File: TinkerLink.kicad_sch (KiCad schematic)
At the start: 28 parts, among them J1 Conn_01x06_Pin, Q2 MMBT2222A, Q3 SQS411ENW-T1_GE3, Q4 SQS411ENW-T1_GE3, SW1 TS-061D-250D4-P, U1 ESP-01F-2M, U2 ME6211C33M5, U3 AP63203WU

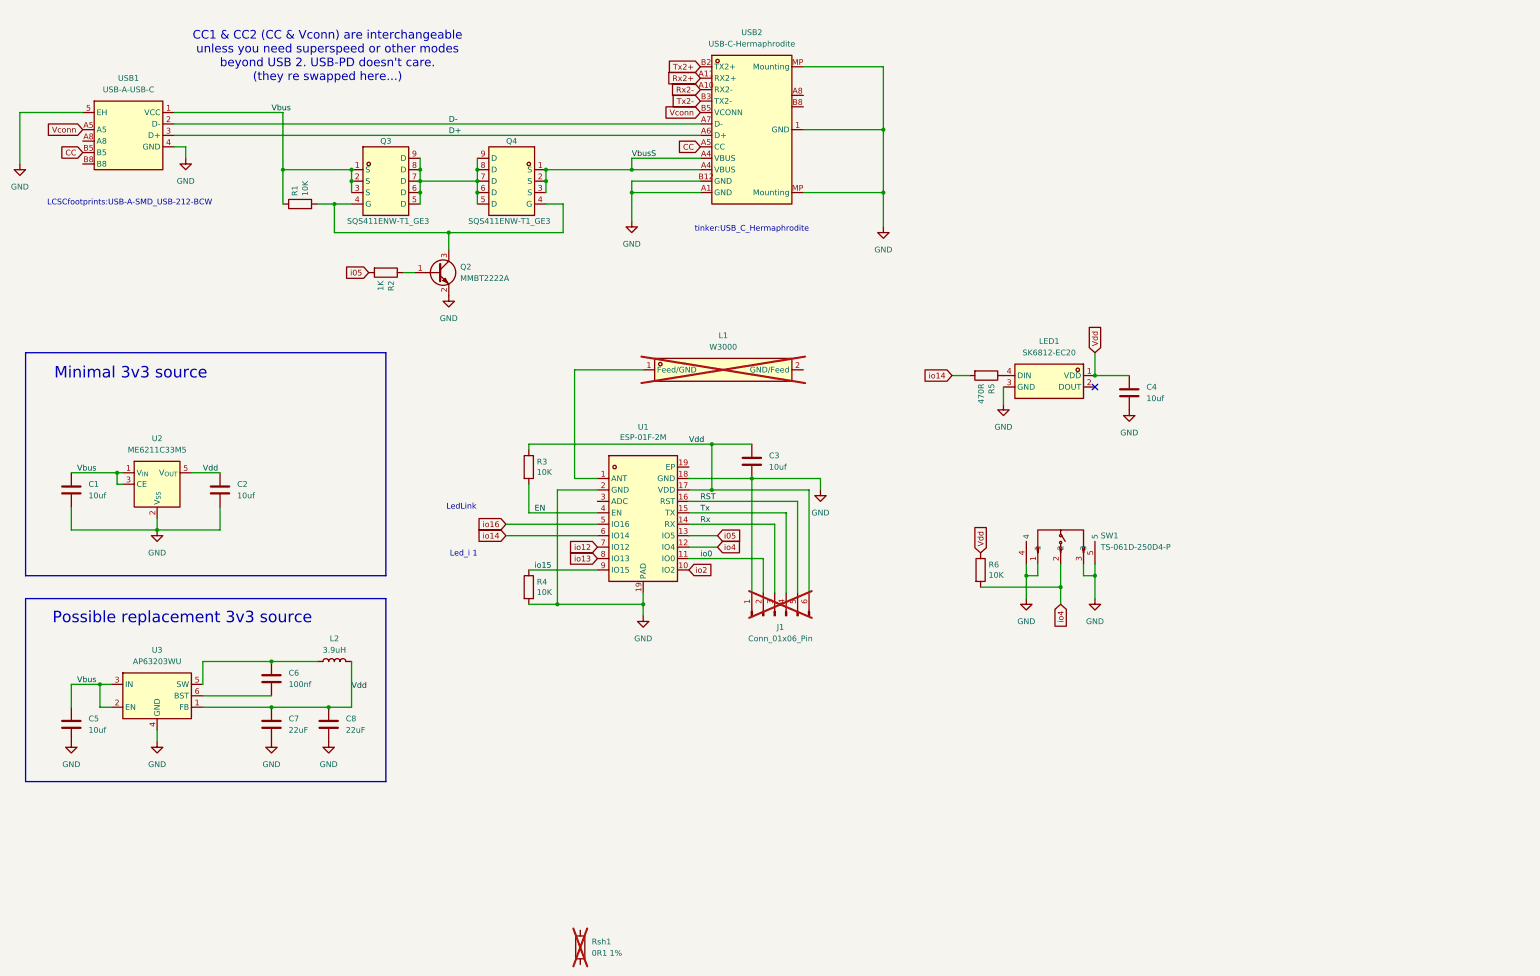
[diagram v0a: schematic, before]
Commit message: upgrades
adds ina228 and 3535 rgbw sk6812 LED
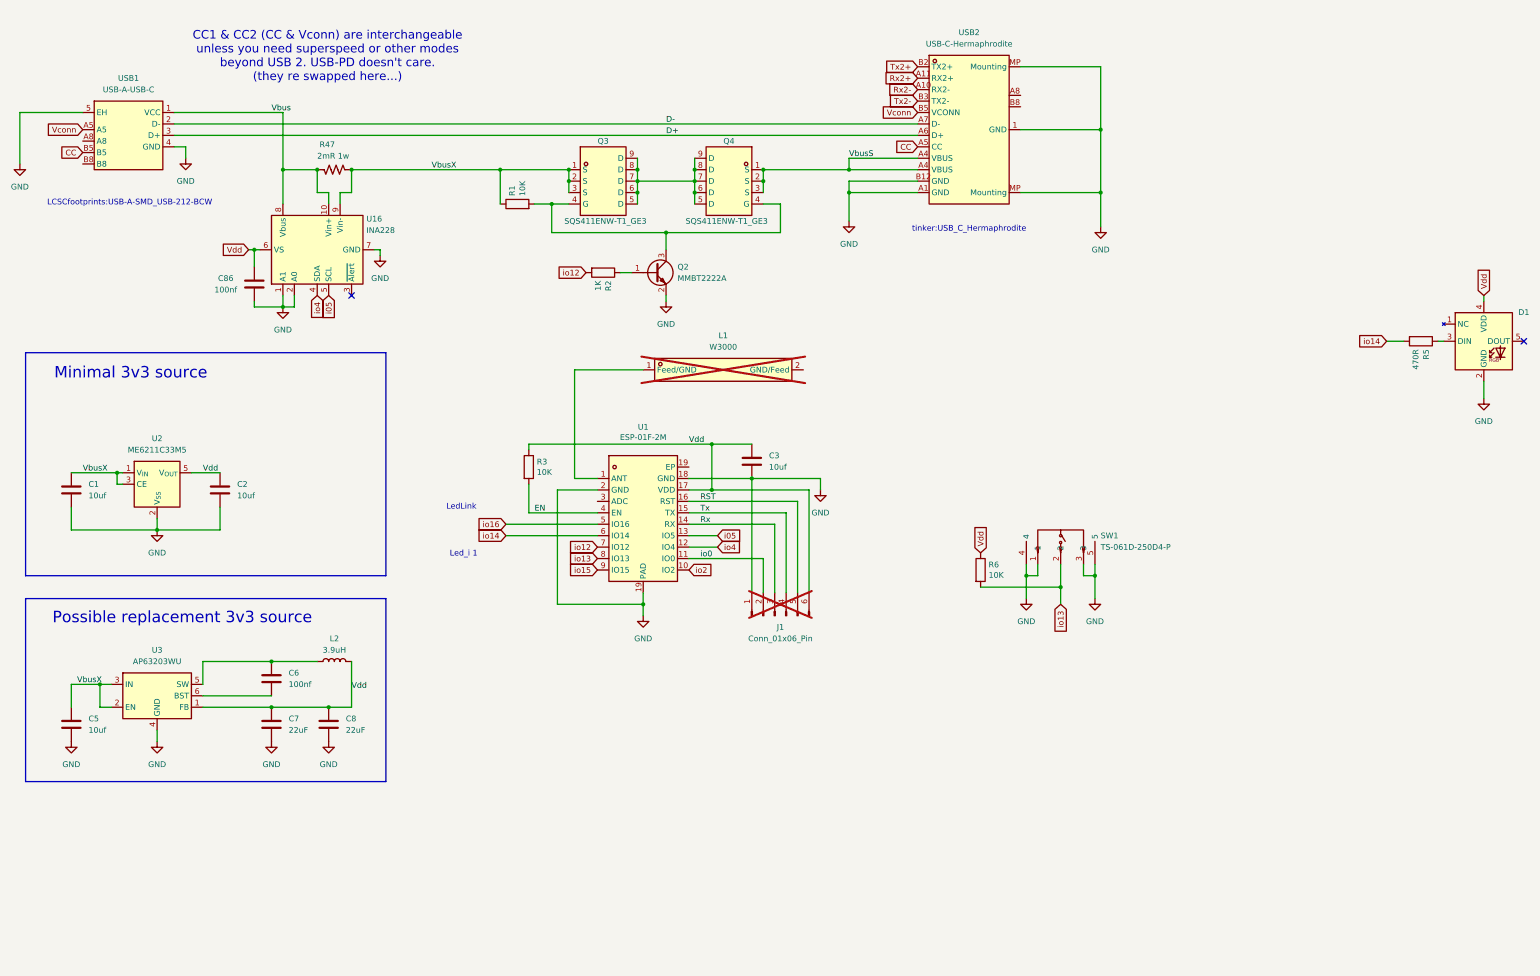
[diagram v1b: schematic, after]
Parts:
- removed C4: 10uf, Capacitor_SMD:C_0603_1608Metric, symbol Device:C
- removed LED1: SK6812-EC20, LCSCfootprints:LED-SMD_4P-L2.0-W2.0-BR, symbol LED-SMD_4P-L2.0-W2.0-BR:SK6812-EC20
- removed R4: 10K, Resistor_SMD:R_0603_1608Metric, symbol Device:R
- removed Rsh1: 0R1 1%, Resistor_SMD:R_2512_6332Metric, symbol Device:R
- added C86: 100nf, Capacitor_SMD:C_0603_1608Metric, symbol Device:C
- added D1: ~, AC_LED:SK6812MINIRGBWNWP6, symbol AC_LED:SK6812_mini_RGBW
- added R47: 2mR 1w, Resistor_SMD:R_1206_3216Metric, symbol Device:R_US
- added U16: INA228, Package_SO:VSSOP-10_3x3mm_P0.5mm, symbol Sensor_Energy:INA228
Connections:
- net GND: now also C86.2, D1.2 (GND), U16.1 (A1), U16.2 (A0), U16.7 (GND)
- net Vbus: now also R47.2, U16.10 (Vin+), U16.8 (Vbus); no longer C1.1, C5.1, Q3.1 (S), Q3.2 (S), Q3.3 (S), R1.1, U2.1 (V_{IN}), U2.3 (CE), U3.2 (EN), U3.3 (IN)
- net Vdd: now also C86.1, D1.4 (VDD), U16.6 (VS)
- net i05: now also U16.5 (SCL); no longer R2.2
- net io12: now also R2.2
- net io13: now also R6.2, SW1.2
- net io4: now also U16.4 (SDA); no longer R6.2, SW1.2
- net at R5.1: now also D1.3 (DIN)
- new net VbusX: C1.1, C5.1, Q3.1 (S), Q3.2 (S), Q3.3 (S), R1.1, R47.1, U16.9 (Vin-), U2.1 (V_{IN}), U2.3 (CE), U3.2 (EN), U3.3 (IN)
- no-connect marks 1 -> 2
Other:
- moved on the sheet: Q2, Q3, Q4, R1, R2, R5, USB2

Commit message: add AC logo
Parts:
- added LOGO1: Creations_logo_med, AC_logos:Creations logo med, symbol AC_logos:Creations_logo_med
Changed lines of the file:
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@@
+	)
+	(symbol
+		(lib_id "AC_logos:Creations_logo_med")
+		(at 19.05 20.32 0)
+		(unit 1)
+		(exclude_from_sim no)
+		(in_bom yes)
+		(on_board yes)
+		(dnp no)
+		(fields_autoplaced yes)
+		(property "Reference" "LOGO1"
+			(at 21.59 19.3039 0)
+			(effects
+				(font
+					(size 1.27 1.27)
+				)
+				(justify left)
+			)
+		)
+		(property "Value" "Creations_logo_med"
+			(at 21.59 21.8439 0)
+			(effects
+				(font
+					(size 1.27 1.27)
+				)
+				(justify left)
+			)
+		)
+		(property "Footprint" "AC_logos:Creations logo med"
+			(at 35.814 23.876 0)
+			(effects
+				(font
+					(size 1.27 1.27)
+				)
+				(hide yes)
+			)
+		)
+		(property "Datasheet" ""
+			(at 19.05 20.32 0)
+			(effects
+				(font
+					(size 1.27 1.27)
+				)
+				(hide yes)
+			)
+		)
+		(property "Description" ""
+			(at 19.05 20.32 0)
+			(effects
+				(font
+					(size 1.27 1.27)
+				)
+				(hide yes)
+			)
+		)
+		(instances
+			(project ""
+				(path "/d9db63b9-0e33-4ffc-b3bb-ae5011fef151"
+					(reference "LOGO1")
+					(unit 1)
+				)
+			)
+		)
 	)
 	(symbol

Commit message: first tweaks post Austin...
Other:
- company: (none) -> S. A. Miller
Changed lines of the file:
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@@
 	(title_block
 		(title "TinkerLink")
-		(rev "0.0.5")
+		(rev "0.0.6")
+		(company "S. A. Miller")
+		(comment 1 "With much input by Austin McNeal")
 	)
 	(rectangle

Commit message: ...
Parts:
- added LED1: SK6812MINIRGBW-WS-P6-A, LCSCfootprints:LED-SMD_6P-L3.5-W3.5_SK6812MINIRGBW-WS-P6-A, symbol C7423106:SK6812MINIRGBW-WS-P6-A
- D1: footprint AC_LED:SK6812MINIRGBWNWP6 -> LCSCfootprints:LED-SMD_6P-L3.5-W3.5_SK6812MINIRGBW-WS-P6-A; now not fitted
- LOGO1: footprint AC_logos:Creations logo med -> LCSCfootprints:Creations logo med
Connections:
- net GND: now also LED1.2 (GND); no longer D1.2 (GND)
- net Vdd: now also LED1.4 (VDD), LED1.6 (VDD); no longer D1.4 (VDD)
- net at R5.1: now also LED1.3 (DIN); no longer D1.3 (DIN)
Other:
- moved on the sheet: R5
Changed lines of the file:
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@@
 	)
 	(junction
+		(at 261.62 93.98)
+		(diameter 0)
+		(color 0 0 0 0)
+	)
+	(junction
 		(at 40.64 115.57)
 		(diameter 0)
@@
 	)
 	(no_connect
-		(at 353.06 86.36)
+		(at 237.49 93.98)
 	)
 	(no_connect
@@
 	(wire
 		(pts
-			(xy 322.58 86.36) (xy 326.39 86.36)
+			(xy 220.98 99.06) (xy 224.79 99.06)
 		)
 		(stroke
@@
 	(wire
 		(pts
+			(xy 236.22 96.52) (xy 236.22 106.68)
+		)
+		(stroke
+			(width 0)
+			(type default)
+		)
+	)
+	(wire
+		(pts
 			(xy 77.47 78.74) (xy 80.01 78.74)
 		)
@@
 	(wire
 		(pts
+			(xy 261.62 99.06) (xy 261.62 93.98)
+		)
+		(stroke
+			(width 0)
+			(type default)
+		)
+	)
+	(wire
+		(pts
 			(xy 77.47 76.2) (xy 77.47 78.74)
 		)
@@
 	(wire
 		(pts
-			(xy 334.01 86.36) (xy 335.28 86.36)
+			(xy 232.41 99.06) (xy 237.49 99.06)
 		)
 		(stroke
@@
 	(wire
 		(pts
+			(xy 257.81 99.06) (xy 261.62 99.06)
+		)
+		(stroke
+			(width 0)
+			(type default)
+		)
+	)
+	(wire
+		(pts
 			(xy 184.15 142.24) (xy 184.15 134.62)
 		)
@@
 	(wire
 		(pts
-			(xy 344.17 76.2) (xy 344.17 77.47)
+			(xy 265.43 93.98) (xy 261.62 93.98)
 		)
 		(stroke
@@
 	(wire
 		(pts
+			(xy 261.62 93.98) (xy 257.81 93.98)
+		)
+		(stroke
+			(width 0)
+			(type default)
+		)
+	)
+	(wire
+		(pts
 			(xy 125.73 48.26) (xy 125.73 55.88)
 		)
@@
 	(wire
 		(pts
+			(xy 237.49 96.52) (xy 236.22 96.52)
+		)
+		(stroke
+			(width 0)
+			(type default)
+		)
+	)
+	(wire
+		(pts
 			(xy 30.48 128.27) (xy 30.48 123.19)
 		)
@@
 	(wire
 		(pts
-			(xy 344.17 95.25) (xy 344.17 99.06)
-		)
-		(stroke
-			(width 0)
-			(type default)
-		)
-	)
-	(wire
-		(pts
 			(xy 71.12 77.47) (xy 71.12 78.74)
 		)
@@
 	(global_label "io14"
 		(shape input)
-		(at 322.58 86.36 180)
+		(at 220.98 99.06 180)
 		(fields_autoplaced yes)
 		(effects
@@
 		)
 		(property "Intersheetrefs" "${INTERSHEET_REFS}"
-			(at 315.422 86.36 0)
+			(at 213.822 99.06 0)
 			(effects
 				(font
@@
 	(global_label "Vdd"
 		(shape input)
-		(at 344.17 76.2 90)
+		(at 265.43 93.98 0)
 		(fields_autoplaced yes)
 		(effects
@@
 		)
 		(property "Intersheetrefs" "${INTERSHEET_REFS}"
-			(at 344.17 69.8282 90)
+			(at 271.8018 93.98 0)
 			(effects
 				(font
@@
 	)
 	(symbol
+		(lib_id "C7423106:SK6812MINIRGBW-WS-P6-A")
+		(at 247.65 96.52 0)
+		(unit 1)
+		(exclude_from_sim no)
+		(in_bom yes)
+		(on_board yes)
+		(dnp no)
+		(fields_autoplaced yes)
+		(property "Reference" "LED1"
+			(at 247.65 86.36 0)
+			(effects
+				(font
+					(size 1.27 1.27)
+				)
+			)
+		)
+		(property "Value" "SK6812MINIRGBW-WS-P6-A"
+			(at 247.65 88.9 0)
+			(effects
+				(font
+					(size 1.27 1.27)
+				)
+			)
+		)
+		(property "Footprint" "LCSCfootprints:LED-SMD_6P-L3.5-W3.5_SK6812MINIRGBW-WS-P6-A"
+			(at 247.65 106.68 0)
+			(effects
+				(font
+					(size 1.27 1.27)
+				)
+				(hide yes)
+			)
+		)
+		(property "Datasheet" "https://www.lcsc.com/datasheet/C7423106.pdf"
+			(at 247.65 109.22 0)
+			(effects
+				(font
+					(size 1.27 1.27)
+				)
+				(hide yes)
+			)
+		)
+		(property "Description" ""
+			(at 247.65 96.52 0)
+			(effects
+				(font
+					(size 1.27 1.27)
+				)
+				(hide yes)
+			)
+		)
+		(property "Manufacturer" "OPSCO(欧思科)"
+			(at 247.65 111.76 0)
+			(effects
+				(font
+					(size 1.27 1.27)
+				)
+				(hide yes)
+			)
+		)
+		(property "MPN" "SK6812MINIRGBW-WS-P6-A"
+			(at 247.65 114.3 0)
+			(effects
+				(font
+					(size 1.27 1.27)
+				)
+				(hide yes)
+			)
+		)
+		(property "LCSC Part" "C7423106"
+			(at 247.65 116.84 0)
+			(effects
+				(font
+					(size 1.27 1.27)
+				)
+				(hide yes)
+			)
+		)
+		(pin "2"
+		)
+		(pin "4"
+		)
+		(pin "3"
+		)
+		(pin "1"
+		)
+		(pin "6"
+		)
+		(pin "5"
+		)
+		(instances
+			(project ""
+				(path "/d9db63b9-0e33-4ffc-b3bb-ae5011fef151"
+					(reference "LED1")
+					(unit 1)
+				)
+			)
+		)
+	)
+	(symbol
 		(lib_id "power:GND")
 		(at 30.48 175.26 0)
@@
 			)
 		)
-		(property "Footprint" "AC_logos:Creations logo med"
+		(property "Footprint" "LCSCfootprints:Creations logo med"
 			(at 35.814 23.876 0)
 			(effects
@@
 	(symbol
 		(lib_id "AC_LED:SK6812_mini_RGBW")
-		(at 344.17 86.36 0)
+		(at 298.45 95.25 0)
 		(unit 1)
 		(exclude_from_sim no)
 		(in_bom yes)
-		(on_board yes)
-		(dnp no)
+		(on_board no)
+		(dnp yes)
 		(fields_autoplaced yes)
 		(property "Reference" "D1"
-			(at 353.06 79.9398 0)
+			(at 307.34 88.8298 0)
 			(effects
 				(font
@@
 		)
 		(property "Value" "~"
-			(at 353.06 82.4798 0)
+			(at 307.34 91.3698 0)
 			(effects
 				(font
@@
 			)
 		)
-		(property "Footprint" "AC_LED:SK6812MINIRGBWNWP6"
-			(at 343.916 108.966 0)
+		(property "Footprint" "LCSCfootprints:LED-SMD_6P-L3.5-W3.5_SK6812MINIRGBW-WS-P6-A"
+			(at 298.196 117.856 0)
 			(effects
 				(font
@@
 		)
 		(property "Datasheet" ""
-			(at 344.17 86.36 0)
+			(at 298.45 95.25 0)
 			(effects
 				(font
@@
 		)
 		(property "Description" "3535 rgbw sk6812 led"
-			(at 344.424 106.68 0)
+			(at 298.704 115.57 0)
 			(effects
 				(font
@@
 		)
 		(property "LCSC" "C7423106"
-			(at 344.17 86.36 0)
+			(at 298.45 95.25 0)
 			(effects
 				(font
@@
 		)
 		(property "warm white" "C7423106"
-			(at 344.17 86.36 0)
+			(at 298.45 95.25 0)
 			(effects
 				(font
@@
 		)
 		(property "cold white" "C7423105"
-			(at 344.17 86.36 0)
+			(at 298.45 95.25 0)
 			(effects
 				(font
@@
 		)
 		(property "neutral white" "C7423107"
-			(at 344.17 86.36 0)
+			(at 298.45 95.25 0)
 			(effects
 				(font
@@
 	(symbol
 		(lib_id "Device:R")
-		(at 330.2 86.36 270)
+		(at 228.6 99.06 270)
 		(unit 1)
 		(exclude_from_sim no)
@@
 		(dnp no)
 		(property "Reference" "R5"
-			(at 331.3684 88.138 0)
+			(at 229.7684 100.838 0)
 			(effects
 				(font
@@
 		)
 		(property "Value" "470R"
-			(at 329.057 88.138 0)
+			(at 227.457 100.838 0)
 			(effects
 				(font
@@
 		)
 		(property "Footprint" "Resistor_SMD:R_0603_1608Metric"
-			(at 330.2 84.582 90)
+			(at 228.6 97.282 90)
 			(effects
 				(font
@@
 		)
 		(property "Datasheet" "~"
-			(at 330.2 86.36 0)
+			(at 228.6 99.06 0)
 			(effects
 				(font
@@
 		)
 		(property "Description" ""
-			(at 330.2 86.36 0)
+			(at 228.6 99.06 0)
 			(effects
 				(font
@@
 		)
 		(property "LCSC Part" "C114433"
-			(at 330.2 86.36 0)
+			(at 228.6 99.06 0)
 			(effects
 				(font
@@
 	(symbol
 		(lib_id "power:GND")
-		(at 344.17 99.06 0)
+		(at 236.22 106.68 0)
 		(unit 1)
 		(exclude_from_sim no)
@@
 		(fields_autoplaced yes)
 		(property "Reference" "#PWR017"
-			(at 344.17 105.41 0)
+			(at 236.22 113.03 0)
 			(effects
 				(font
@@
 		)
 		(property "Value" "GND"
-			(at 344.17 104.14 0)
+			(at 236.22 111.76 0)
 			(effects
 				(font
@@
 		)
 		(property "Footprint" ""
-			(at 344.17 99.06 0)
+			(at 236.22 106.68 0)
 			(effects
 				(font
@@
 		)
 		(property "Datasheet" ""
-			(at 344.17 99.06 0)
+			(at 236.22 106.68 0)
 			(effects
 				(font
@@
 		)
 		(property "Description" "Power symbol creates a global label with name \"GND\" , ground"
-			(at 344.17 99.06 0)
+			(at 236.22 106.68 0)
 			(effects
 				(font

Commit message: ...
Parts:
- LOGO1: footprint LCSCfootprints:Creations logo med -> AUSTINfootprints:Creations logo med
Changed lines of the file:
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@@
 			)
 		)
-		(property "Footprint" "LCSCfootprints:Creations logo med"
+		(property "Footprint" "AUSTINfootprints:Creations logo med"
 			(at 35.814 23.876 0)
 			(effects

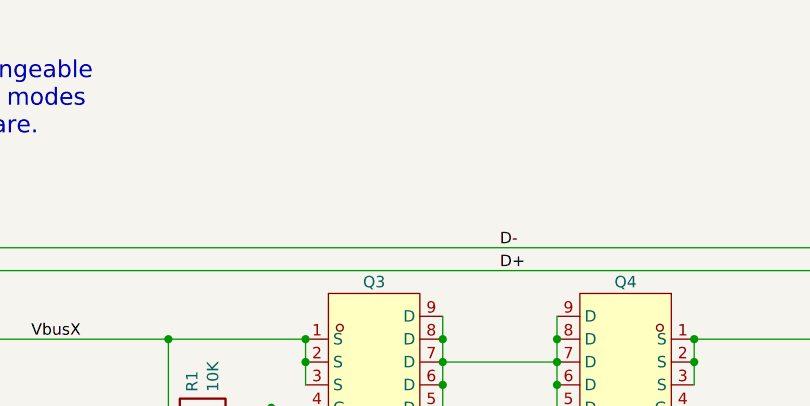
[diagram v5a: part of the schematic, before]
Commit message: Added TPD2EUSB30A to D+/D- for ESD protection
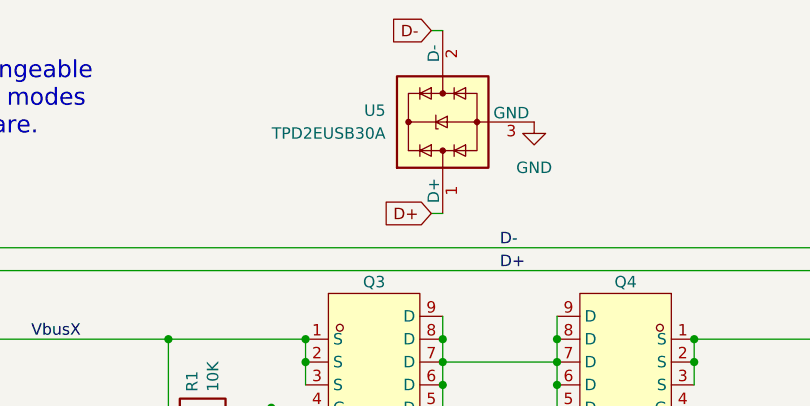
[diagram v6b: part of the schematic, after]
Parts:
- added U5: TPD2EUSB30A, Package_TO_SOT_SMD:Texas_DRT-3, symbol Power_Protection:TPD2EUSB30A
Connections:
- net D+: now also U5.1 (D+)
- net D-: now also U5.2 (D-)
- net GND: now also U5.3 (GND)
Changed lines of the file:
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@@
 	(wire
 		(pts
+			(xy 154.94 34.29) (xy 156.21 34.29)
+		)
+		(stroke
+			(width 0)
+			(type default)
+		)
+	)
+	(wire
+		(pts
 			(xy 156.21 53.34) (xy 156.21 55.88)
 		)
@@
 	(wire
 		(pts
+			(xy 154.94 13.97) (xy 156.21 13.97)
+		)
+		(stroke
+			(width 0)
+			(type default)
+		)
+	)
+	(wire
+		(pts
 			(xy 87.63 167.64) (xy 92.71 167.64)
 		)
@@
 		)
 	)
+	(global_label "D-"
+		(shape input)
+		(at 154.94 13.97 180)
+		(fields_autoplaced yes)
+		(effects
+			(font
+				(size 1.27 1.27)
+			)
+			(justify right)
+		)
+		(property "Intersheetrefs" "${INTERSHEET_REFS}"
+			(at 149.1124 13.97 0)
+			(effects
+				(font
+					(size 1.27 1.27)
+				)
+				(justify right)
+				(hide yes)
+			)
+		)
+	)
 	(global_label "CC"
 		(shape input)
@@
 		)
 	)
+	(global_label "D+"
+		(shape input)
+		(at 154.94 34.29 180)
+		(fields_autoplaced yes)
+		(effects
+			(font
+				(size 1.27 1.27)
+			)
+			(justify right)
+		)
+		(property "Intersheetrefs" "${INTERSHEET_REFS}"
+			(at 149.1124 34.29 0)
+			(effects
+				(font
+					(size 1.27 1.27)
+				)
+				(justify right)
+				(hide yes)
+			)
+		)
+	)
 	(global_label "io16"
 		(shape input)
@@
 	(symbol
 		(lib_id "power:GND")
+		(at 166.37 24.13 0)
+		(unit 1)
+		(exclude_from_sim no)
+		(in_bom yes)
+		(on_board yes)
+		(dnp no)
+		(fields_autoplaced yes)
+		(property "Reference" "#PWR022"
+			(at 166.37 30.48 0)
+			(effects
+				(font
+					(size 1.27 1.27)
+				)
+				(hide yes)
+			)
+		)
+		(property "Value" "GND"
+			(at 166.37 29.21 0)
+			(effects
+				(font
+					(size 1.27 1.27)
+				)
+			)
+		)
+		(property "Footprint" ""
+			(at 166.37 24.13 0)
+			(effects
+				(font
+					(size 1.27 1.27)
+				)
+				(hide yes)
+			)
+		)
+		(property "Datasheet" ""
+			(at 166.37 24.13 0)
+			(effects
+				(font
+					(size 1.27 1.27)
+				)
+				(hide yes)
+			)
+		)
+		(property "Description" "Power symbol creates a global label with name \"GND\" , ground"
+			(at 166.37 24.13 0)
+			(effects
+				(font
+					(size 1.27 1.27)
+				)
+				(hide yes)
+			)
+		)
+		(pin "1"
+		)
+		(instances
+			(project "TinkerLink"
+				(path "/d9db63b9-0e33-4ffc-b3bb-ae5011fef151"
+					(reference "#PWR022")
+					(unit 1)
+				)
+			)
+		)
+	)
+	(symbol
+		(lib_id "power:GND")
 		(at 162.56 77.47 0)
 		(unit 1)
@@
 					(unit 1)
 				)
+			)
+		)
+	)
+	(symbol
+		(lib_id "Power_Protection:TPD2EUSB30A")
+		(at 156.21 24.13 90)
+		(unit 1)
+		(exclude_from_sim no)
+		(in_bom yes)
+		(on_board yes)
+		(dnp no)
+		(property "Reference" "U5"
+			(at 149.86 22.8599 90)
+			(effects
+				(font
+					(size 1.27 1.27)
+				)
+				(justify left)
+			)
+		)
+		(property "Value" "TPD2EUSB30A"
+			(at 149.86 25.3999 90)
+			(effects
+				(font
+					(size 1.27 1.27)
+				)
+				(justify left)
+			)
+		)
+		(property "Footprint" "Package_TO_SOT_SMD:Texas_DRT-3"
+			(at 163.83 43.18 0)
+			(effects
+				(font
+					(size 1.27 1.27)
+				)
+				(hide yes)
+			)
+		)
+		(property "Datasheet" "http://www.ti.com/lit/ds/symlink/tpd2eusb30a.pdf"
+			(at 156.21 24.13 0)
+			(effects
+				(font
+					(size 1.27 1.27)
+				)
+				(hide yes)
+			)
+		)
+		(property "Description" "2-Channel ESD Protection for Super-Speed USB 3.0 Interface, DRT-3"
+			(at 156.21 24.13 0)
+			(effects
+				(font
+					(size 1.27 1.27)
+				)
+				(hide yes)
+			)
+		)
+		(property "LCSC Part" "C3011197"
+			(at 156.21 24.13 90)
+			(effects
+				(font
+					(size 1.27 1.27)
+				)
+				(hide yes)
+			)
+		)
+		(property "LCSC part" ""
+			(at 156.21 24.13 90)
+			(effects
+				(font
+					(size 1.27 1.27)
+				)
+				(hide yes)
+			)
+		)
+		(pin "2"
+		)
+		(pin "3"
+		)
+		(pin "1"
+		)
+		(instances
+			(project "TinkerLink"
+				(path "/d9db63b9-0e33-4ffc-b3bb-ae5011fef151"
+					(reference "U5")
+					(unit 1)
+				)
